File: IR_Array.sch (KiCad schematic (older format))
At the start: 14 parts, among them Q1 AO3400A

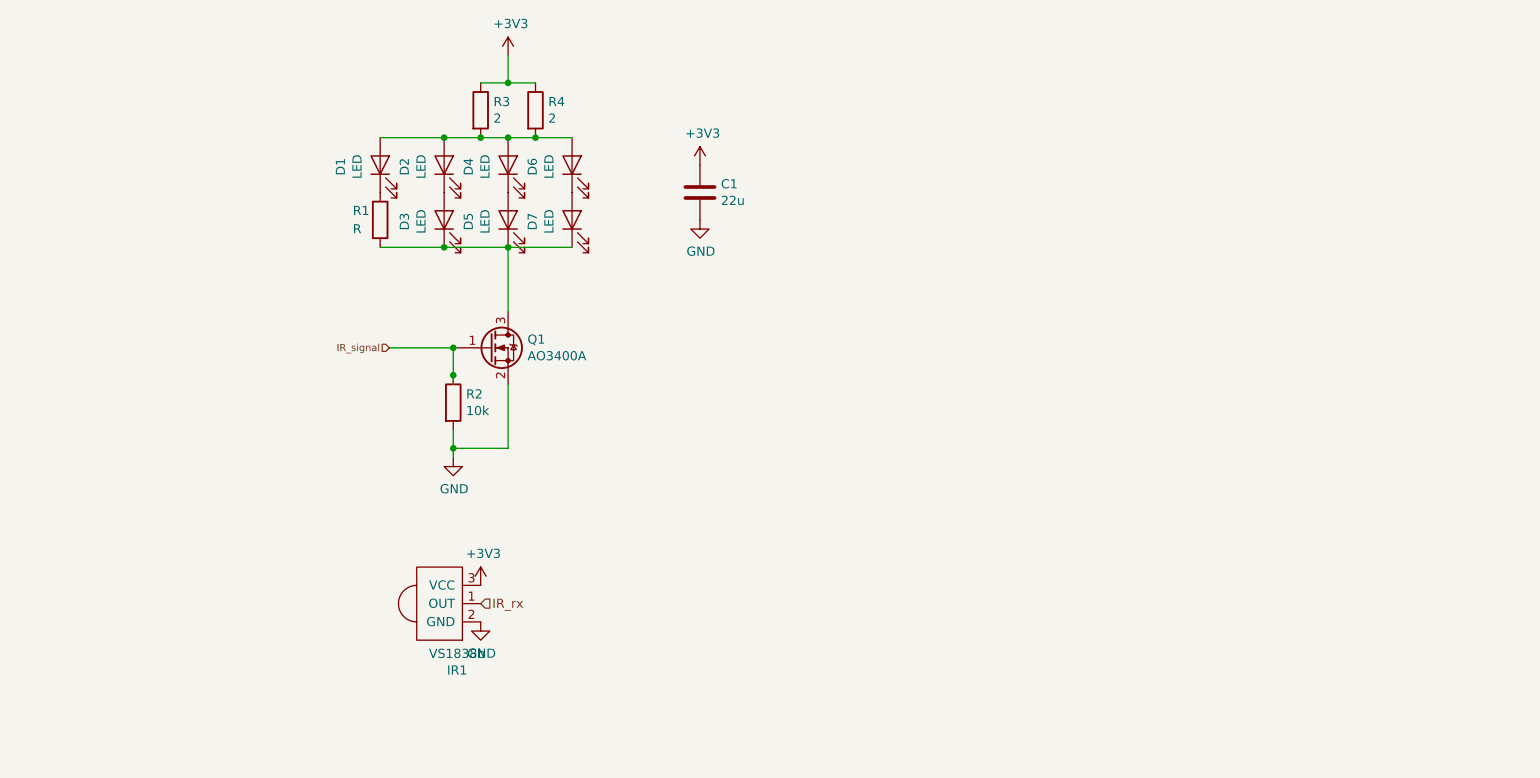
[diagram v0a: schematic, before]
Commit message: add boost converter, IR RX, 433MHz RX/TX and labels
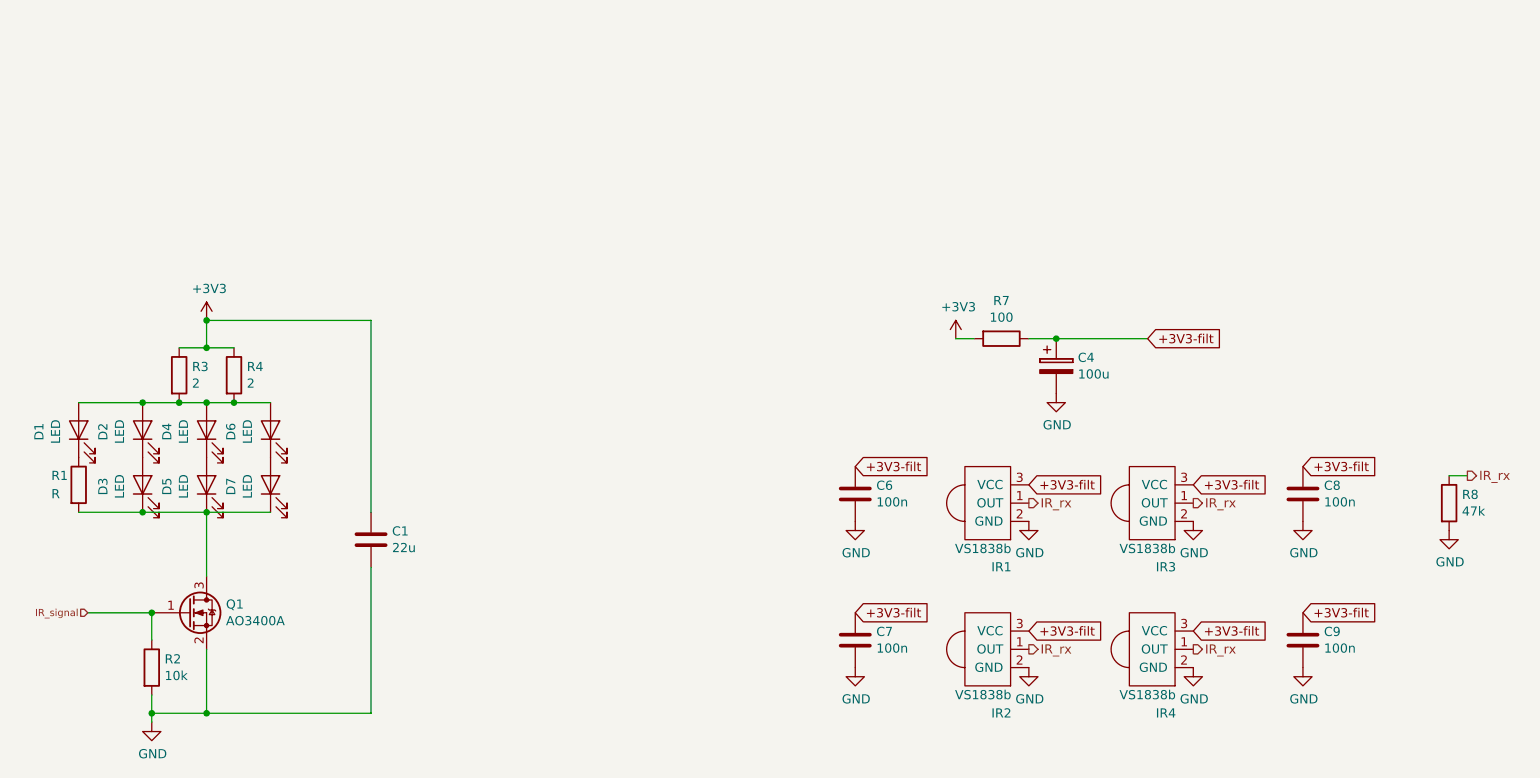
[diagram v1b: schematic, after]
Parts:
- added C4: 100u, Capacitor_SMD:CP_Elec_6.3x5.8, symbol Device:CP
- added C6, C7, C8, C9: 100n, LeoDJ-kicad:C_0805_2012Metric, symbol Device:C
- added IR2, IR3, IR4: VS1838b, LeoDJ-kicad:VS1838b, symbol LeoDJ-kicad:VS1838b
- added R7: 100, LeoDJ-kicad:R_0805_2012Metric, symbol Device:R
- added R8: 47k, LeoDJ-kicad:R_0805_2012Metric, symbol Device:R
- D2, D3, D4, D5, D6, D7: footprint LED_THT:LED_D5.0mm_Horizontal_O1.27mm_Z9.0mm -> LeoDJ-kicad:LED_D5.0mm_Horizontal_O1.27mm_Z9.0mm
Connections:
- net labels added: +3V3-filt
- wire segments 19 -> 26
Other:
- moved on the sheet: C1, D1, D2, D3, D4, D5, D6, D7, IR1, Q1, R1, R2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
